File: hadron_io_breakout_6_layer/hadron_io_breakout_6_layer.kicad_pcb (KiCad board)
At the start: 6 copper layers, 83.2 x 21.9 mm, 18 parts, among them J1 TF38-18S-0.5SV_830_, J2 SFM-110-02-L-D-A, J3 TF38-18S-0.5SV_830_, J4 SAMTEC-SFM-120-02-L-D-A, J5 SM04B-NSHSS-TB_LF__SN_, J6 SM08B-NSHSS-TB LFSN, J7 Conn_01x03_Pin

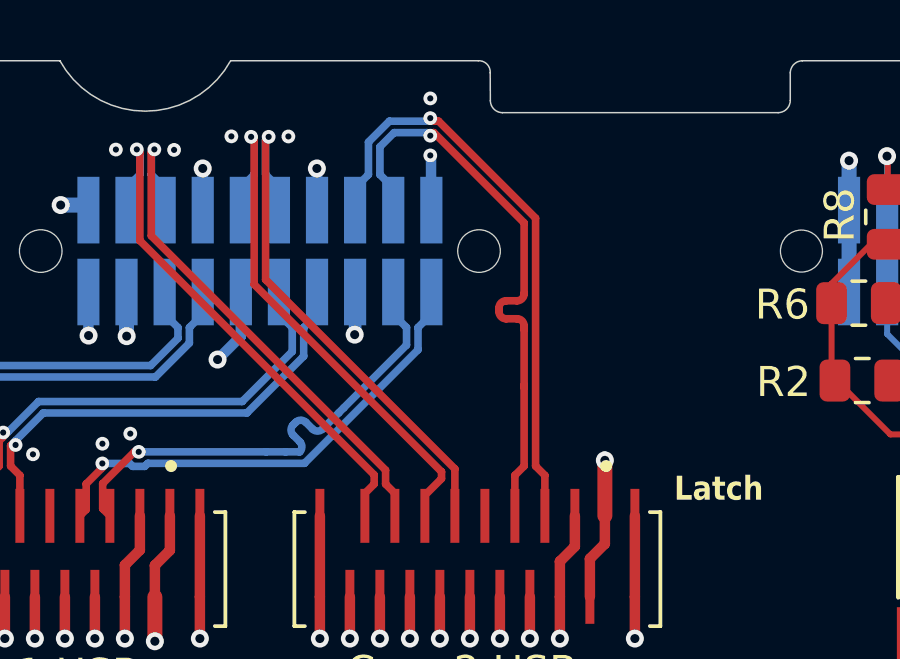
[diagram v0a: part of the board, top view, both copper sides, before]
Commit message: Updated hadron_io_breakout with <ahem> differential crossover
Fixed issue where I wasn't crossing over SS differential lines. Still need to review prior to manufacture.
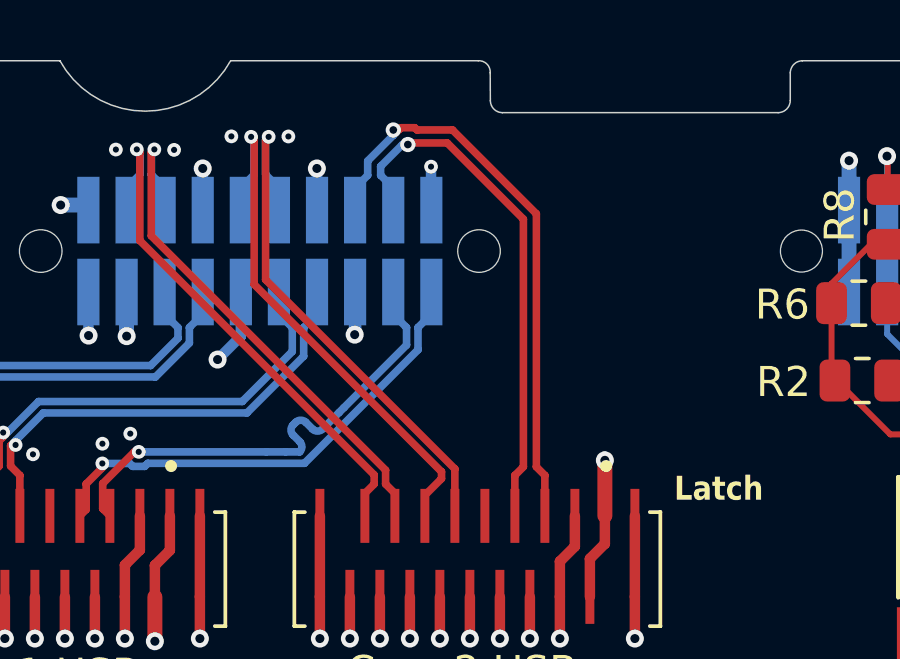
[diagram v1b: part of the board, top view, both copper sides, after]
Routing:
- net USB0_D_P: track 19.7 -> 17.8 mm
- net GND: track 81.4 -> 81.0 mm, vias 46 -> 45
